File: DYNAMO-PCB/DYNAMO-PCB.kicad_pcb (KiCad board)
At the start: 2 copper layers, 1 part

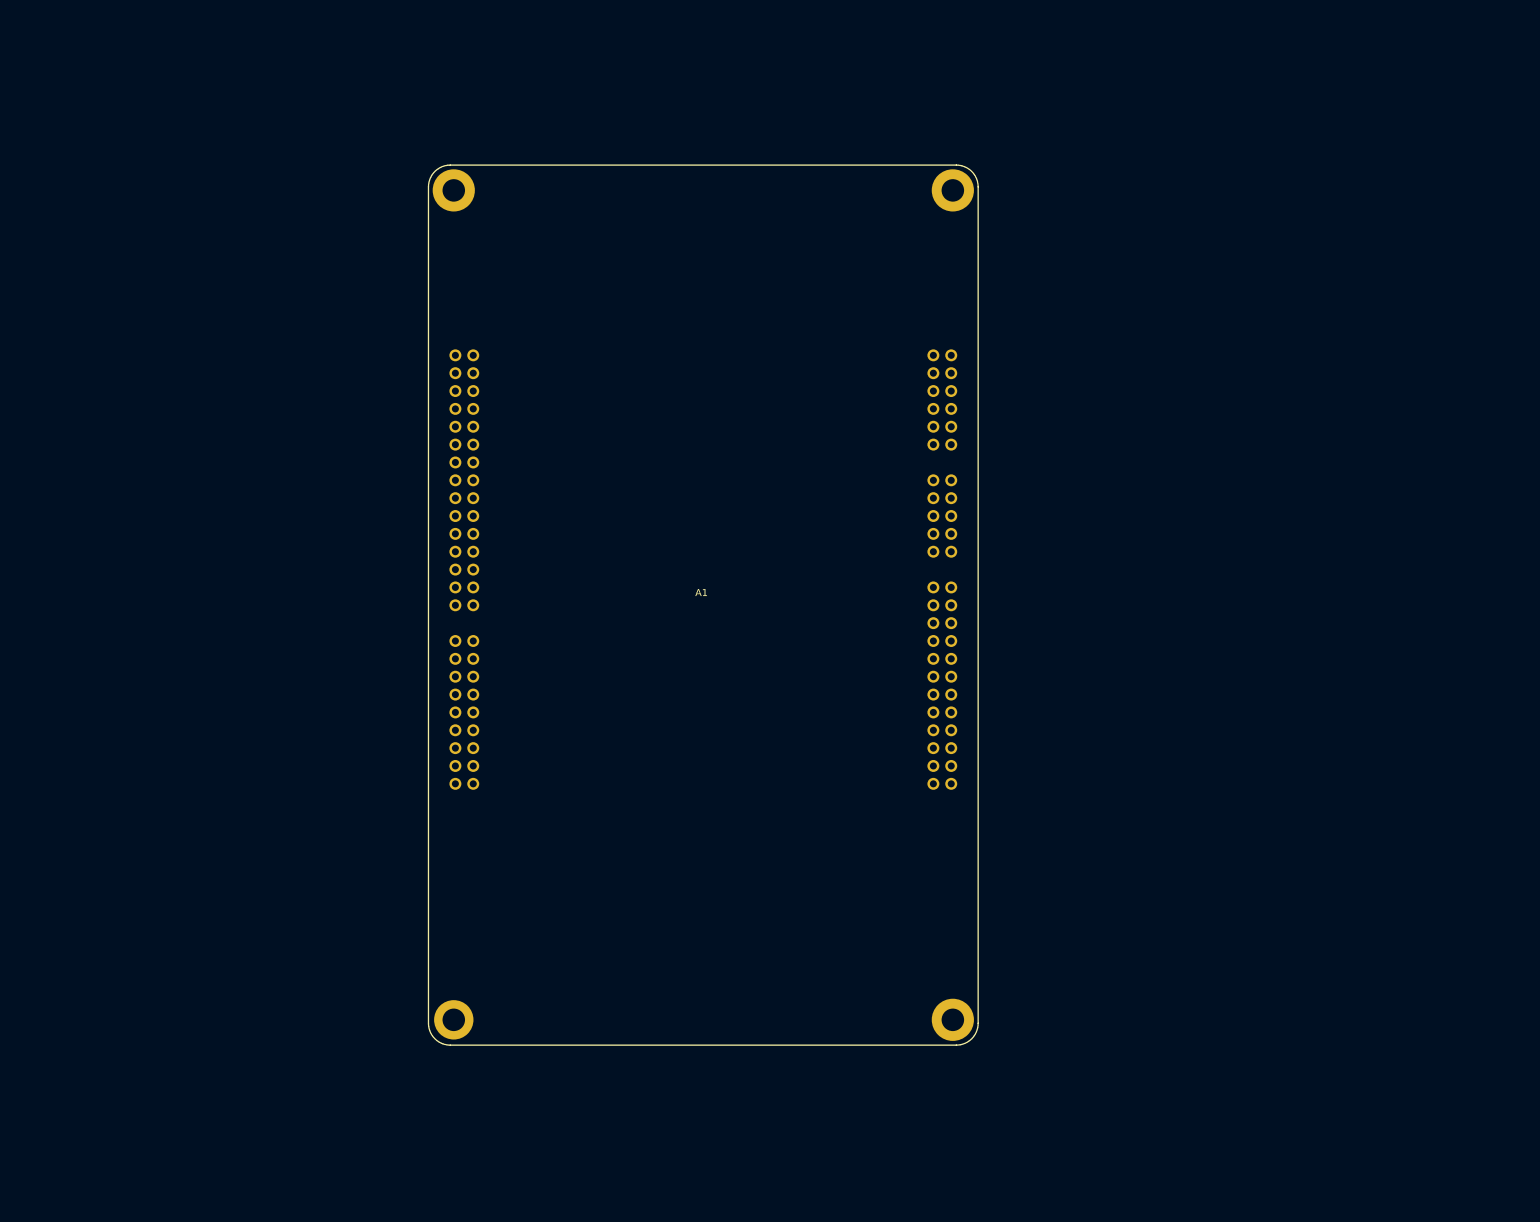
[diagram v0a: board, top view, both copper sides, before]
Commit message: footprint assignments
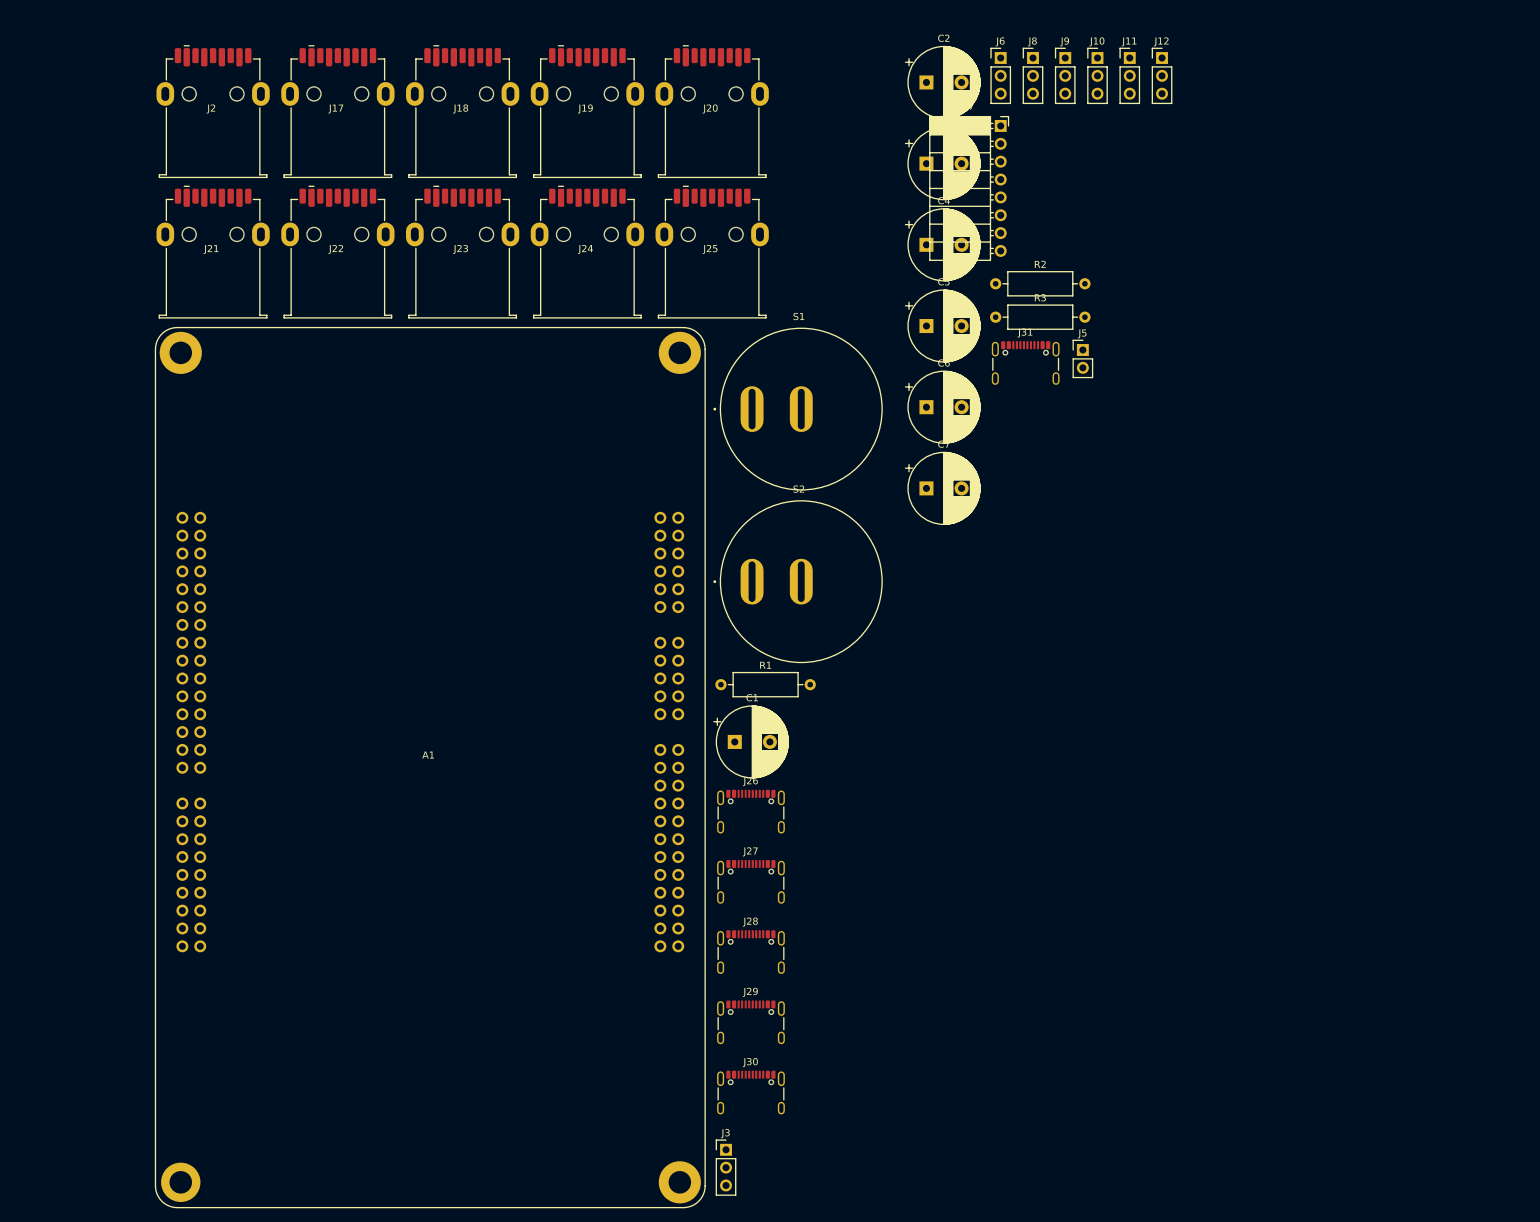
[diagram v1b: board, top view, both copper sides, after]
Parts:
- added C1: C_Polarized, Capacitor_THT:CP_Radial_D10.0mm_P5.00mm, F.Cu at (147.0, 117.9)
- added C2: C_Polarized, Capacitor_THT:CP_Radial_D10.0mm_P5.00mm, F.Cu at (174.2, 24.0)
- added C3: C_Polarized, Capacitor_THT:CP_Radial_D10.0mm_P5.00mm, F.Cu at (174.2, 35.6)
- added C4: C_Polarized, Capacitor_THT:CP_Radial_D10.0mm_P5.00mm, F.Cu at (174.2, 47.1)
- added C5: C_Polarized, Capacitor_THT:CP_Radial_D10.0mm_P5.00mm, F.Cu at (174.2, 58.7)
- added C6: C_Polarized, Capacitor_THT:CP_Radial_D10.0mm_P5.00mm, F.Cu at (174.2, 70.2)
- added C7: C_Polarized, Capacitor_THT:CP_Radial_D10.0mm_P5.00mm, F.Cu at (174.2, 81.8)
- added J10: Conn_01x03_Pin, Connector_PinHeader_2.54mm:PinHeader_1x03_P2.54mm_Vertical, F.Cu at (198.6, 20.6)
- added J11: Conn_01x03_Pin, Connector_PinHeader_2.54mm:PinHeader_1x03_P2.54mm_Vertical, F.Cu at (203.2, 20.6)
- added J12: Conn_01x03_Pin, Connector_PinHeader_2.54mm:PinHeader_1x03_P2.54mm_Vertical, F.Cu at (207.8, 20.6)
- added J17: USB3_A, 692122030100:692122030100, F.Cu at (90.3, 28.2)
- added J18: USB3_A, 692122030100:692122030100, F.Cu at (108.1, 28.2)
- added J19: USB3_A, 692122030100:692122030100, F.Cu at (125.8, 28.2)
- added J2: USB3_A, 692122030100:692122030100, F.Cu at (72.6, 28.2)
- added J20: USB3_A, 692122030100:692122030100, F.Cu at (143.6, 28.2)
- added J21: USB3_A, 692122030100:692122030100, F.Cu at (72.6, 48.2)
- added J22: USB3_A, 692122030100:692122030100, F.Cu at (90.3, 48.2)
- added J23: USB3_A, 692122030100:692122030100, F.Cu at (108.1, 48.2)
- added J24: USB3_A, 692122030100:692122030100, F.Cu at (125.8, 48.2)
- added J25: USB3_A, 692122030100:692122030100, F.Cu at (143.6, 48.2)
- added J26: USB_C_Receptacle_USB2.0_16P, Connector_USB:USB_C_Receptacle_GCT_USB4105-xx-A_16P_TopMnt_Horizontal, F.Cu at (149.3, 128.9)
- added J27: USB_C_Receptacle_USB2.0_16P, Connector_USB:USB_C_Receptacle_GCT_USB4105-xx-A_16P_TopMnt_Horizontal, F.Cu at (149.3, 138.9)
- added J28: USB_C_Receptacle_USB2.0_16P, Connector_USB:USB_C_Receptacle_GCT_USB4105-xx-A_16P_TopMnt_Horizontal, F.Cu at (149.3, 148.9)
- added J29: USB_C_Receptacle_USB2.0_16P, Connector_USB:USB_C_Receptacle_GCT_USB4105-xx-A_16P_TopMnt_Horizontal, F.Cu at (149.3, 158.9)
- added J3: Conn_01x03_Pin, Connector_PinHeader_2.54mm:PinHeader_1x03_P2.54mm_Vertical, F.Cu at (145.7, 175.9)
- added J30: USB_C_Receptacle_USB2.0_16P, Connector_USB:USB_C_Receptacle_GCT_USB4105-xx-A_16P_TopMnt_Horizontal, F.Cu at (149.3, 168.9)
- added J31: USB_C_Receptacle_USB2.0_16P, Connector_USB:USB_C_Receptacle_GCT_USB4105-xx-A_16P_TopMnt_Horizontal, F.Cu at (188.4, 65.1)
- added J5: Conn_01x02_Pin, Connector_PinHeader_2.54mm:PinHeader_1x02_P2.54mm_Vertical, F.Cu at (196.5, 62.1)
- added J6: Conn_01x03_Pin, Connector_PinHeader_2.54mm:PinHeader_1x03_P2.54mm_Vertical, F.Cu at (184.8, 20.6)
- added J7: Conn_01x08_Socket, Connector_PinSocket_2.54mm:PinSocket_1x08_P2.54mm_Horizontal, F.Cu at (184.8, 30.2)
- added J8: Conn_01x03_Pin, Connector_PinHeader_2.54mm:PinHeader_1x03_P2.54mm_Vertical, F.Cu at (189.4, 20.6)
- added J9: Conn_01x03_Pin, Connector_PinHeader_2.54mm:PinHeader_1x03_P2.54mm_Vertical, F.Cu at (194.0, 20.6)
- added R1: R, Resistor_THT:R_Axial_DIN0309_L9.0mm_D3.2mm_P12.70mm_Horizontal, F.Cu at (145.0, 109.7)
- added R2: R, Resistor_THT:R_Axial_DIN0309_L9.0mm_D3.2mm_P12.70mm_Horizontal, F.Cu at (184.1, 52.7)
- added R3: R, Resistor_THT:R_Axial_DIN0309_L9.0mm_D3.2mm_P12.70mm_Horizontal, F.Cu at (184.1, 57.4)
- added S1: RR511D1121, RR511D1121:E-SWITCH_RR511D1121, F.Cu at (156.4, 70.5)
- added S2: RR511D1121, RR511D1121:E-SWITCH_RR511D1121, F.Cu at (156.4, 95.1)
- moved A1 45.2 mm to (68.4, 86.0)

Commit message: schematic wip
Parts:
- removed C6, C7: C_Polarized, Capacitor_THT:CP_Radial_D10.0mm_P5.00mm
- added J1: HDMI_A, Connector_Video:HDMI_A_Molex_208658-1001_Horizontal, F.Cu at (140.0, 88.5)
- added J13: Conn_01x02_Pin, Connector_PinHeader_2.54mm:PinHeader_1x02_P2.54mm_Vertical, F.Cu at (183.5, 81.8)
- added J32: USB3_A, 692122030100:692122030100, F.Cu at (178.6, 69.4)
- added U1: TPS65988DHRSHR, TPS65988DHRSHR:IC_TPS65987DDHRSHR, F.Cu at (195.1, 157.9)
- added U2: CH7035B-BF, CH7035B-BF:QFN40P1000X1000X90-89N, F.Cu at (213.0, 144.9)
- added U3: USB7206/KDX, ul_USB7206-KDX:VQFN100_KDX_MCH, F.Cu at (197.0, 146.1)
- moved J30 118.2 mm to (220.8, 74.7)
- moved J26 110.4 mm to (220.8, 44.8)
- moved J27 110.4 mm to (220.8, 54.8)
- moved J28 110.4 mm to (220.8, 64.8)
- moved J3 99.8 mm to (178.9, 81.8)
- moved J11 96.6 mm to (222.1, 115.3)
- moved J12 96.6 mm to (226.7, 115.3)
- moved J10 96.6 mm to (217.6, 115.3)
- moved J6 96.6 mm to (203.8, 115.3)
- moved J8 96.6 mm to (208.4, 115.3)
- moved J9 96.6 mm to (213.0, 115.3)
- moved J29 77.2 mm to (170.8, 84.7)
- moved R2 74.8 mm to (203.1, 125.0)
- moved R3 74.8 mm to (203.1, 129.8)
- moved C2 74.8 mm to (193.2, 96.4)
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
